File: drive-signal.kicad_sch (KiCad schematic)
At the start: 25 parts, among them J1 Conn_01x03_Pin, J10 Conn_01x04_Pin, J11 Conn_01x04_Pin, J2 Conn_01x03_Pin, J3 Conn_01x03_Pin, J4 Conn_01x03_Pin, J5 JETSON, J6 IMU, J7 Conn_01x02_Pin, J8 Conn_01x04_Pin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

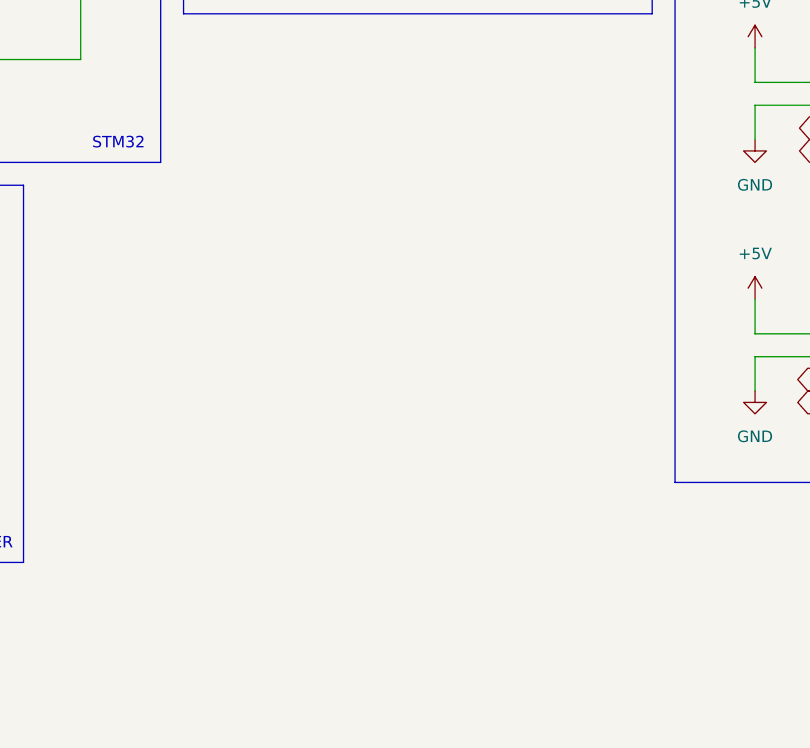
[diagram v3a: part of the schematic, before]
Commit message: add mounting holes with pads
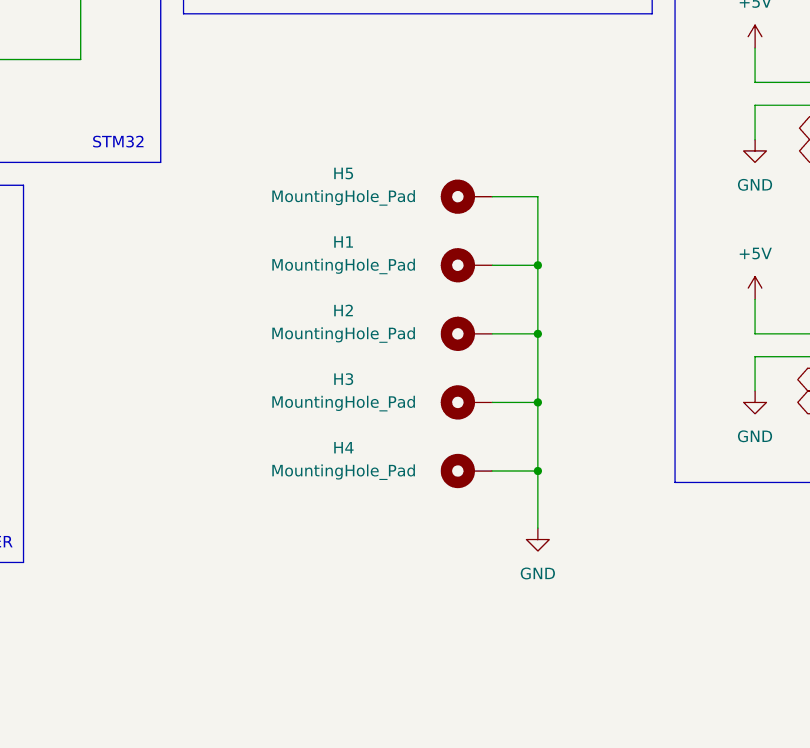
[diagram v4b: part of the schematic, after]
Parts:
- added H1, H2, H3, H4, H5: MountingHole_Pad, MountingHole:MountingHole_3.2mm_M3_Pad_Via, symbol Mechanical:MountingHole_Pad
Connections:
- net GND: now also H1.1, H2.1, H3.1, H4.1, H5.1
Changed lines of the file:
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@@
   (junction (at 26.67 172.72) (diameter 0) (color 0 0 0 0)
   )
+  (junction (at 181.61 123.19) (diameter 0) (color 0 0 0 0)
+  )
   (junction (at 185.42 60.96) (diameter 0) (color 0 0 0 0)
   )
@@
   (junction (at 185.42 38.1) (diameter 0) (color 0 0 0 0)
   )
+  (junction (at 181.61 130.81) (diameter 0) (color 0 0 0 0)
+  )
   (junction (at 26.67 166.37) (diameter 0) (color 0 0 0 0)
   )
+  (junction (at 181.61 107.95) (diameter 0) (color 0 0 0 0)
+  )
   (junction (at 92.71 119.38) (diameter 0) (color 0 0 0 0)
   )
   (junction (at 26.67 160.02) (diameter 0) (color 0 0 0 0)
+  )
+  (junction (at 181.61 115.57) (diameter 0) (color 0 0 0 0)
   )
   (no_connect (at 107.95 63.5))
@@
     (stroke (width 0) (type default))
   )
+  (wire (pts (xy 181.61 115.57) (xy 176.53 115.57))
+    (stroke (width 0) (type default))
+  )
   (wire (pts (xy 35.56 179.07) (xy 38.1 179.07))
     (stroke (width 0) (type default))
@@
     (stroke (width 0) (type default))
   )
+  (wire (pts (xy 181.61 130.81) (xy 176.53 130.81))
+    (stroke (width 0) (type default))
+  )
   (wire (pts (xy 123.19 71.12) (xy 123.19 72.39))
     (stroke (width 0) (type default))
@@
     (stroke (width 0) (type default))
   )
+  (wire (pts (xy 181.61 100.33) (xy 176.53 100.33))
+    (stroke (width 0) (type default))
+  )
   (wire (pts (xy 107.95 53.34) (xy 111.76 53.34))
     (stroke (width 0) (type default))
@@
     (stroke (width 0) (type default))
   )
+  (wire (pts (xy 181.61 107.95) (xy 181.61 115.57))
+    (stroke (width 0) (type default))
+  )
   (wire (pts (xy 76.2 53.34) (xy 80.01 53.34))
     (stroke (width 0) (type default))
@@
     (stroke (width 0) (type default))
   )
+  (wire (pts (xy 181.61 115.57) (xy 181.61 123.19))
+    (stroke (width 0) (type default))
+  )
   (wire (pts (xy 81.28 119.38) (xy 92.71 119.38))
     (stroke (width 0) (type default))
@@
     (stroke (width 0) (type default))
   )
+  (wire (pts (xy 181.61 130.81) (xy 181.61 137.16))
+    (stroke (width 0) (type default))
+  )
   (wire (pts (xy 167.64 60.96) (xy 171.45 60.96))
     (stroke (width 0) (type default))
@@
     (stroke (width 0) (type default))
   )
+  (wire (pts (xy 181.61 107.95) (xy 176.53 107.95))
+    (stroke (width 0) (type default))
+  )
   (wire (pts (xy 76.2 60.96) (xy 80.01 60.96))
     (stroke (width 0) (type default))
@@
     (stroke (width 0) (type default))
   )
+  (wire (pts (xy 181.61 123.19) (xy 181.61 130.81))
+    (stroke (width 0) (type default))
+  )
   (wire (pts (xy 154.94 49.53) (xy 160.02 49.53))
     (stroke (width 0) (type default))
@@
     (stroke (width 0) (type default))
   )
+  (wire (pts (xy 181.61 100.33) (xy 181.61 107.95))
+    (stroke (width 0) (type default))
+  )
   (wire (pts (xy 205.74 121.92) (xy 205.74 118.11))
     (stroke (width 0) (type default))
@@
   )
   (wire (pts (xy 205.74 30.48) (xy 222.25 30.48))
+    (stroke (width 0) (type default))
+  )
+  (wire (pts (xy 181.61 123.19) (xy 176.53 123.19))
     (stroke (width 0) (type default))
   )
@@
     )
   )
+  (symbol (lib_id "Mechanical:MountingHole_Pad") (at 173.99 115.57 90) (unit 1)
+    (in_bom yes) (on_board yes) (dnp no)
+    (property "Reference" "H2" (at 160.02 113.03 90)
+      (effects (font (size 1.27 1.27)))
+    )
+    (property "Value" "MountingHole_Pad" (at 160.02 115.57 90)
+      (effects (font (size 1.27 1.27)))
+    )
+    (property "Footprint" "MountingHole:MountingHole_3.2mm_M3_Pad_Via" (at 173.99 115.57 0)
+      (effects (font (size 1.27 1.27)) hide)
+    )
+    (property "Datasheet" "~" (at 173.99 115.57 0)
+      (effects (font (size 1.27 1.27)) hide)
+    )
+    (pin "1")
+    (instances
+      (project "drive-signal"
+        (path "/0fd5a227-32c1-4fb8-b9b0-22b52f16b2f2"
+          (reference "H2") (unit 1)
+        )
+      )
+    )
+  )
   (symbol (lib_id "Connector:Conn_01x04_Pin") (at 227.33 120.65 180) (unit 1)
     (in_bom yes) (on_board yes) (dnp no) (fields_autoplaced)
@@
         (path "/0fd5a227-32c1-4fb8-b9b0-22b52f16b2f2"
           (reference "D3") (unit 1)
+        )
+      )
+    )
+  )
+  (symbol (lib_id "Mechanical:MountingHole_Pad") (at 173.99 123.19 90) (unit 1)
+    (in_bom yes) (on_board yes) (dnp no)
+    (property "Reference" "H3" (at 160.02 120.65 90)
+      (effects (font (size 1.27 1.27)))
+    )
+    (property "Value" "MountingHole_Pad" (at 160.02 123.19 90)
+      (effects (font (size 1.27 1.27)))
+    )
+    (property "Footprint" "MountingHole:MountingHole_3.2mm_M3_Pad_Via" (at 173.99 123.19 0)
+      (effects (font (size 1.27 1.27)) hide)
+    )
+    (property "Datasheet" "~" (at 173.99 123.19 0)
+      (effects (font (size 1.27 1.27)) hide)
+    )
+    (pin "1")
+    (instances
+      (project "drive-signal"
+        (path "/0fd5a227-32c1-4fb8-b9b0-22b52f16b2f2"
+          (reference "H3") (unit 1)
         )
       )
@@
     )
   )
+  (symbol (lib_id "Mechanical:MountingHole_Pad") (at 173.99 107.95 90) (unit 1)
+    (in_bom yes) (on_board yes) (dnp no)
+    (property "Reference" "H1" (at 160.02 105.41 90)
+      (effects (font (size 1.27 1.27)))
+    )
+    (property "Value" "MountingHole_Pad" (at 160.02 107.95 90)
+      (effects (font (size 1.27 1.27)))
+    )
+    (property "Footprint" "MountingHole:MountingHole_3.2mm_M3_Pad_Via" (at 173.99 107.95 0)
+      (effects (font (size 1.27 1.27)) hide)
+    )
+    (property "Datasheet" "~" (at 173.99 107.95 0)
+      (effects (font (size 1.27 1.27)) hide)
+    )
+    (pin "1")
+    (instances
+      (project "drive-signal"
+        (path "/0fd5a227-32c1-4fb8-b9b0-22b52f16b2f2"
+          (reference "H1") (unit 1)
+        )
+      )
+    )
+  )
   (symbol (lib_id "power:+5V") (at 205.74 55.88 0) (unit 1)
     (in_bom yes) (on_board yes) (dnp no) (fields_autoplaced)
@@
     )
   )
+  (symbol (lib_id "Mechanical:MountingHole_Pad") (at 173.99 130.81 90) (unit 1)
+    (in_bom yes) (on_board yes) (dnp no)
+    (property "Reference" "H4" (at 160.02 128.27 90)
+      (effects (font (size 1.27 1.27)))
+    )
+    (property "Value" "MountingHole_Pad" (at 160.02 130.81 90)
+      (effects (font (size 1.27 1.27)))
+    )
+    (property "Footprint" "MountingHole:MountingHole_3.2mm_M3_Pad_Via" (at 173.99 130.81 0)
+      (effects (font (size 1.27 1.27)) hide)
+    )
+    (property "Datasheet" "~" (at 173.99 130.81 0)
+      (effects (font (size 1.27 1.27)) hide)
+    )
+    (pin "1")
+    (instances
+      (project "drive-signal"
+        (path "/0fd5a227-32c1-4fb8-b9b0-22b52f16b2f2"
+          (reference "H4") (unit 1)
+        )
+      )
+    )
+  )
   (symbol (lib_id "power:PWR_FLAG") (at 81.28 111.76 0) (unit 1)
     (in_bom yes) (on_board yes) (dnp no) (fields_autoplaced)
@@
         (path "/0fd5a227-32c1-4fb8-b9b0-22b52f16b2f2"
           (reference "#PWR02") (unit 1)
+        )
+      )
+    )
+  )
+  (symbol (lib_id "Mechanical:MountingHole_Pad") (at 173.99 100.33 90) (unit 1)
+    (in_bom yes) (on_board yes) (dnp no)
+    (property "Reference" "H5" (at 160.02 97.79 90)
+      (effects (font (size 1.27 1.27)))
+    )
+    (property "Value" "MountingHole_Pad" (at 160.02 100.33 90)
+      (effects (font (size 1.27 1.27)))
+    )
+    (property "Footprint" "MountingHole:MountingHole_3.2mm_M3_Pad_Via" (at 173.99 100.33 0)
+      (effects (font (size 1.27 1.27)) hide)
+    )
+    (property "Datasheet" "~" (at 173.99 100.33 0)
+      (effects (font (size 1.27 1.27)) hide)
+    )
+    (pin "1")
+    (instances
+      (project "drive-signal"
+        (path "/0fd5a227-32c1-4fb8-b9b0-22b52f16b2f2"
+          (reference "H5") (unit 1)
         )
       )
@@
         )
       )
+    )
+  )
+  (symbol (lib_id "power:GND") (at 181.61 137.16 0) (unit 1)
+    (in_bom yes) (on_board yes) (dnp no) (fields_autoplaced)
+    (property "Reference" "#PWR026" (at 181.61 143.51 0)
+      (effects (font (size 1.27 1.27)) hide)
+    )
+    (property "Value" "GND" (at 181.61 142.24 0)
+      (effects (font (size 1.27 1.27)))
+    )
+    (property "Footprint" "" (at 181.61 137.16 0)
+      (effects (font (size 1.27 1.27)) hide)
+    )
+    (property "Datasheet" "" (at 181.61 137.16 0)
+      (effects (font (size 1.27 1.27)) hide)
+    )
+    (pin "1")
+    (instances
+      (project "drive-signal"
+        (path "/0fd5a227-32c1-4fb8-b9b0-22b52f16b2f2"
+          (reference "#PWR026") (unit 1)
+        )
+      )

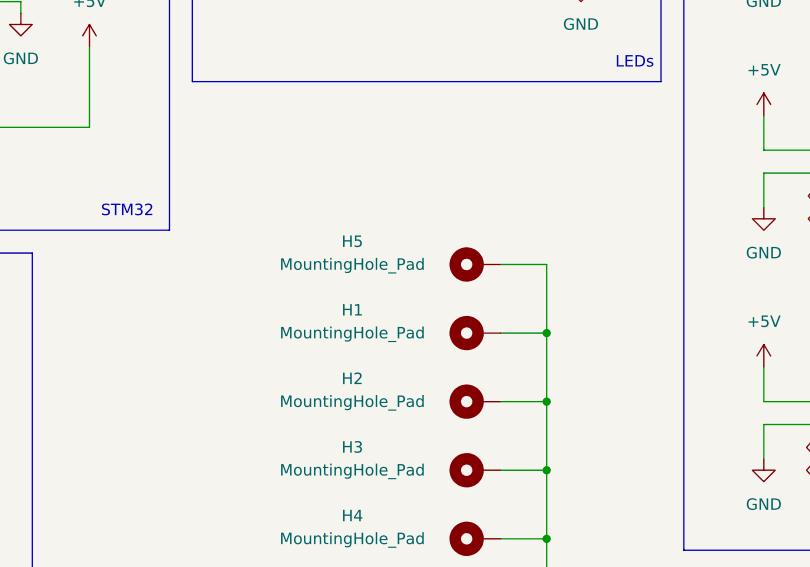
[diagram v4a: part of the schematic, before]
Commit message: reduce mounting holes
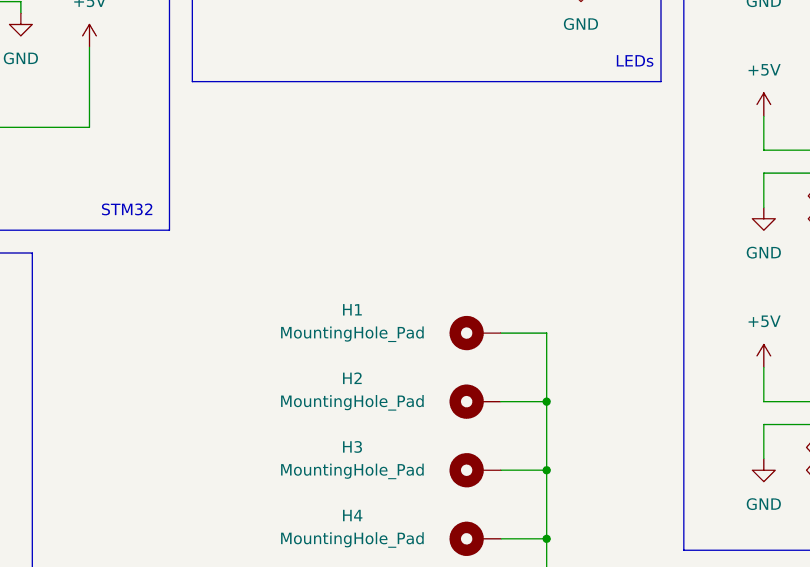
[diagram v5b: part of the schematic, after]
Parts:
- removed H5: MountingHole_Pad, MountingHole:MountingHole_3.2mm_M3_Pad_Via, symbol Mechanical:MountingHole_Pad
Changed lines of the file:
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@@
   (junction (at 26.67 166.37) (diameter 0) (color 0 0 0 0)
-  )
-  (junction (at 181.61 107.95) (diameter 0) (color 0 0 0 0)
   )
   (junction (at 92.71 119.38) (diameter 0) (color 0 0 0 0)
@@
     (stroke (width 0) (type default))
   )
-  (wire (pts (xy 181.61 100.33) (xy 176.53 100.33))
-    (stroke (width 0) (type default))
-  )
   (wire (pts (xy 107.95 53.34) (xy 111.76 53.34))
     (stroke (width 0) (type default))
@@
   )
   (wire (pts (xy 26.67 19.05) (xy 30.48 19.05))
-    (stroke (width 0) (type default))
-  )
-  (wire (pts (xy 181.61 100.33) (xy 181.61 107.95))
     (stroke (width 0) (type default))
   )
@@
         )
       )
-    )
-  )
-  (symbol (lib_id "Mechanical:MountingHole_Pad") (at 173.99 100.33 90) (unit 1)
-    (in_bom yes) (on_board yes) (dnp no)
-    (property "Reference" "H5" (at 160.02 97.79 90)
-      (effects (font (size 1.27 1.27)))
-    )
-    (property "Value" "MountingHole_Pad" (at 160.02 100.33 90)
-      (effects (font (size 1.27 1.27)))
-    )
-    (property "Footprint" "MountingHole:MountingHole_3.2mm_M3_Pad_Via" (at 173.99 100.33 0)
-      (effects (font (size 1.27 1.27)) hide)
-    )
-    (property "Datasheet" "~" (at 173.99 100.33 0)
-      (effects (font (size 1.27 1.27)) hide)
-    )
-    (pin "1")
-    (instances
-      (project "drive-signal"
-        (path "/0fd5a227-32c1-4fb8-b9b0-22b52f16b2f2"
-          (reference "H5") (unit 1)
-        )
-      )

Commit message: done placement
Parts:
- added J12: IMU, Connector_PinHeader_2.54mm:PinHeader_1x08_P2.54mm_Vertical, symbol Connector:Conn_01x08_Pin
- added J13: I2C2 P1, Connector_JST:JST_EH_S3B-EH_1x03_P2.50mm_Horizontal, symbol Connector:Conn_01x03_Pin
- added J14: I2C2 P2, Connector_JST:JST_EH_S3B-EH_1x03_P2.50mm_Horizontal, symbol Connector:Conn_01x03_Pin
- J1, J2, J3, J4: footprint Connector_JST:JST_PH_S3B-PH-K_1x03_P2.00mm_Horizontal -> Connector_JST:JST_EH_S3B-EH_1x03_P2.50mm_Horizontal
- J10, J11, J8, J9: footprint Connector_JST:JST_PH_S4B-PH-K_1x04_P2.00mm_Horizontal -> Connector_JST:JST_EH_S4B-EH_1x04_P2.50mm_Horizontal
- J5: footprint Connector_JST:JST_PH_B3B-PH-K_1x03_P2.00mm_Vertical -> Connector_JST:JST_EH_B3B-EH-A_1x03_P2.50mm_Vertical
- J6: footprint Connector_JST:JST_PH_B4B-PH-K_1x04_P2.00mm_Vertical -> Connector_JST:JST_EH_B4B-EH-A_1x04_P2.50mm_Vertical
- J7: footprint Connector_JST:JST_PH_B2B-PH-K_1x02_P2.00mm_Vertical -> Connector_JST:JST_EH_B2B-EH-A_1x02_P2.50mm_Vertical
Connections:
- net +5V: now also J12.1 (Pin_1)
- net GND: now also J12.2 (Pin_2), J13.1 (Pin_1), J14.1 (Pin_1)
- net I2C1_I_SCL: now also J12.3 (Pin_3)
- net I2C1_I_SDA: now also J12.4 (Pin_4)
- net I2C2_J_SCL: now also J13.3 (Pin_3), J14.3 (Pin_3)
- net I2C2_J_SDA: now also J13.2 (Pin_2), J14.2 (Pin_2)
- no-connect marks 16 -> 20
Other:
- moved on the sheet: H1, H2, H3, H4

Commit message: vias and cleanup
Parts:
- J7: value Conn_01x02_Pin -> POWER
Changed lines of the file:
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@@
       (effects (font (size 1.27 1.27)) (justify right))
     )
-    (property "Value" "Conn_01x02_Pin" (at 101.6 121.92 0)
+    (property "Value" "POWER" (at 101.6 121.92 0)
       (effects (font (size 1.27 1.27)) (justify right))
     )
